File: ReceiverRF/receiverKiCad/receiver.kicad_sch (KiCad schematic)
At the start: 23 parts, among them J2 Conn_01x05_Socket, U1 STM32F103RET6, Y1 Crystal_GND24

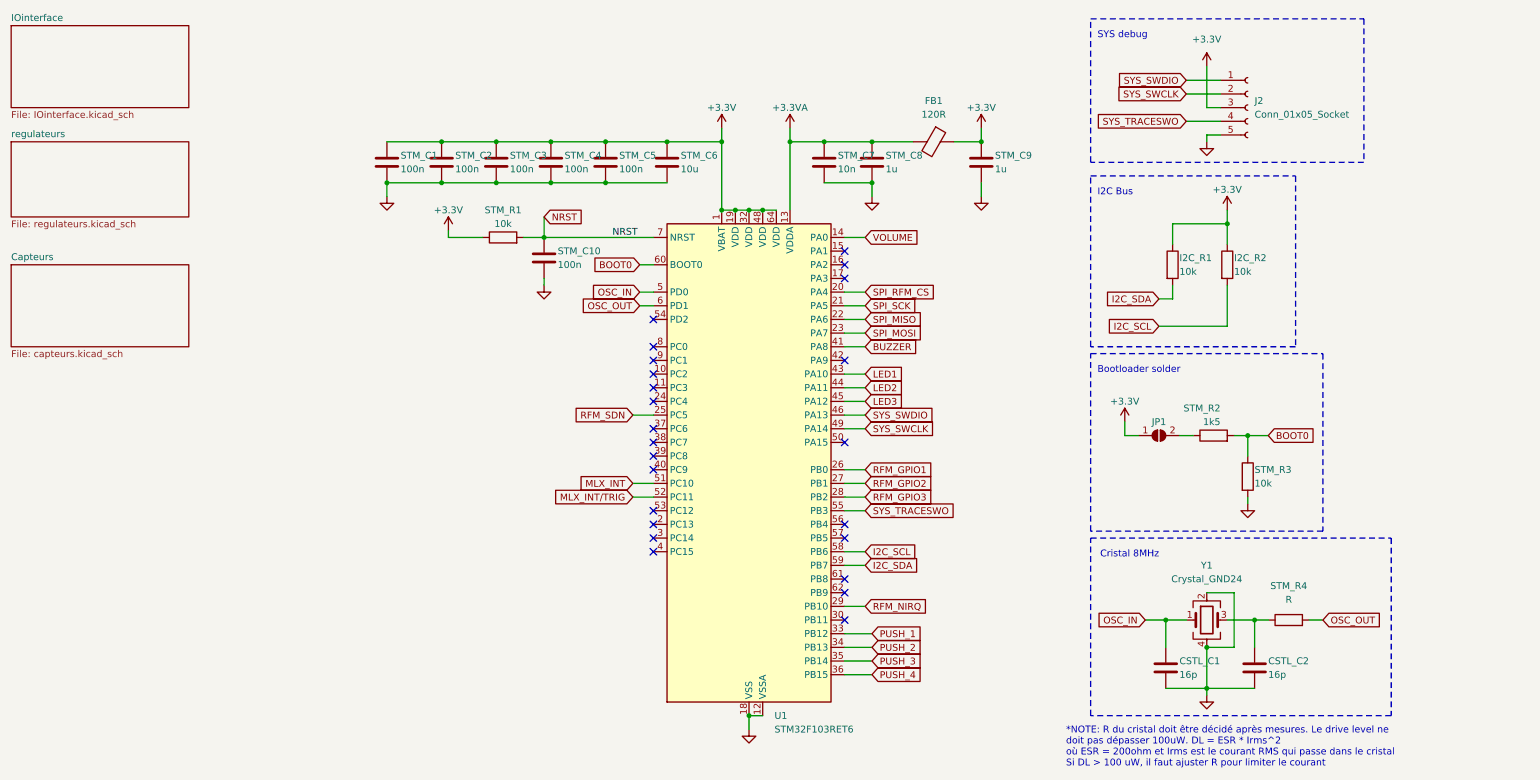
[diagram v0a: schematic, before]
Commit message: impédance 50 ohm pour l'Antenne
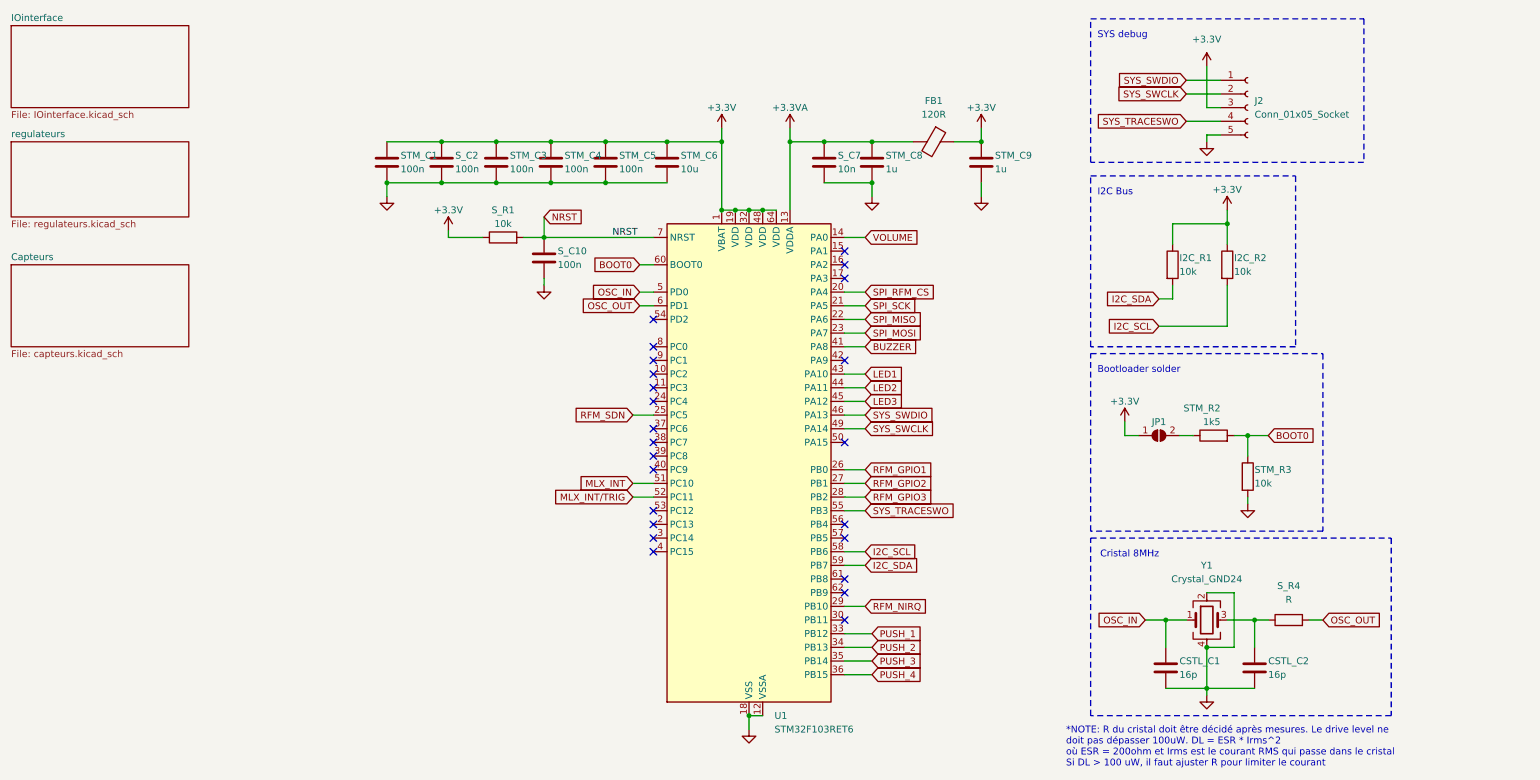
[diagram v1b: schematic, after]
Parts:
- renumbered STM_C10 to S_C10, STM_C2 to S_C2, STM_C7 to S_C7, STM_R1 to S_R1, STM_R4 to S_R4
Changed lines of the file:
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@@
 		(on_board yes)
 		(dnp no)
-		(property "Reference" "STM_R1"
+		(property "Reference" "S_R1"
 			(at 107.95 49.53 90)
 			(effects
@@
 			(project "receiver"
 				(path "/439ba515-58d4-4b14-87ab-b438dcf423a5"
-					(reference "STM_R1")
+					(reference "S_R1")
 					(unit 1)
 				)
@@
 		(on_board yes)
 		(dnp no)
-		(property "Reference" "STM_C2"
+		(property "Reference" "S_C2"
 			(at 99.06 39.37 0)
 			(effects
@@
 			(project "receiver"
 				(path "/439ba515-58d4-4b14-87ab-b438dcf423a5"
-					(reference "STM_C2")
+					(reference "S_C2")
 					(unit 1)
 				)
@@
 		(dnp no)
 		(fields_autoplaced yes)
-		(property "Reference" "STM_R4"
+		(property "Reference" "S_R4"
 			(at 254 119.38 90)
 			(effects
@@
 			(project "receiver"
 				(path "/439ba515-58d4-4b14-87ab-b438dcf423a5"
-					(reference "STM_R4")
+					(reference "S_R4")
 					(unit 1)
 				)
@@
 		(on_board yes)
 		(dnp no)
-		(property "Reference" "STM_C7"
+		(property "Reference" "S_C7"
 			(at 170.18 39.37 0)
 			(effects
@@
 			(project "receiver"
 				(path "/439ba515-58d4-4b14-87ab-b438dcf423a5"
-					(reference "STM_C7")
+					(reference "S_C7")
 					(unit 1)
 				)
@@
 		(on_board yes)
 		(dnp no)
-		(property "Reference" "STM_C10"
+		(property "Reference" "S_C10"
 			(at 118.11 57.15 0)
 			(effects
@@
 			(project "receiver"
 				(path "/439ba515-58d4-4b14-87ab-b438dcf423a5"
-					(reference "STM_C10")
-					(unit 1)
-				)
+					(reference "S_C10")
+					(unit 1)
+				)

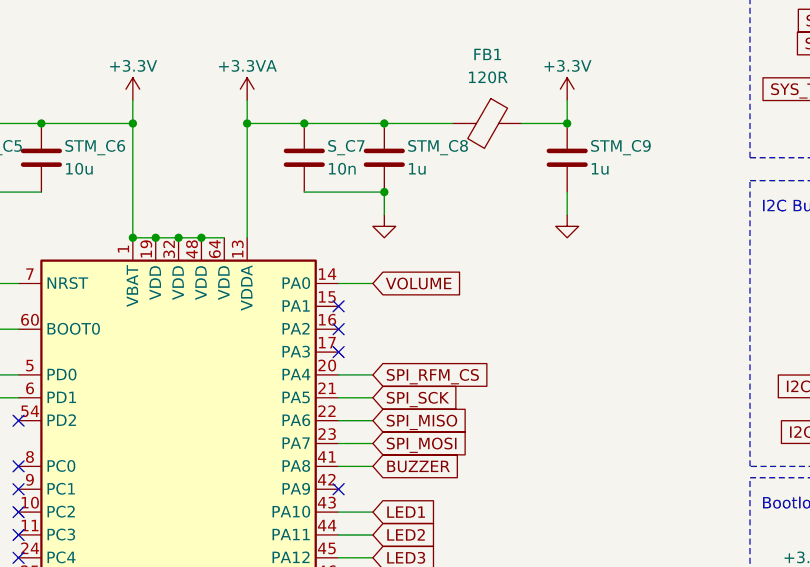
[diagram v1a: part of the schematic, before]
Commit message: changement circuit volume du buzzer. Ajustement du volume direct plutot que software.
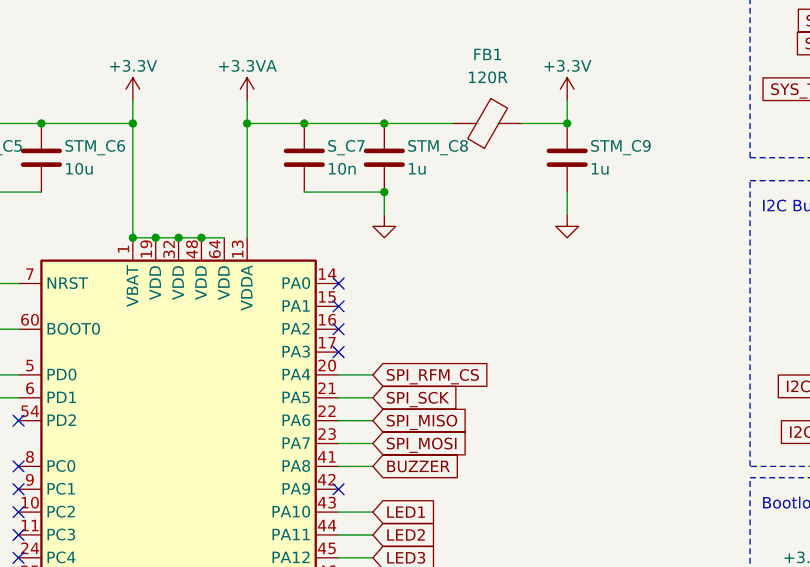
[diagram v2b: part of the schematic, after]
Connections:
- net VOLUME: no longer names the net of U1.14 (PA0)
- no-connect marks 24 -> 25
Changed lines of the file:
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@@
+	)
+	(no_connect
+		(at 135.89 95.25)
+	)
+	(no_connect
+		(at 171.45 59.69)
+	)
+	(no_connect
+		(at 171.45 77.47)
+	)
+	(no_connect
+		(at 135.89 105.41)
+	)
+	(no_connect
+		(at 135.89 85.09)
+	)
+	(no_connect
+		(at 135.89 110.49)
+	)
+	(no_connect
+		(at 171.45 120.65)
 	)
 	(no_connect
@@
 	)
 	(no_connect
-		(at 135.89 95.25)
-	)
-	(no_connect
-		(at 171.45 59.69)
-	)
-	(no_connect
-		(at 171.45 77.47)
-	)
-	(no_connect
-		(at 135.89 105.41)
-	)
-	(no_connect
-		(at 135.89 85.09)
-	)
-	(no_connect
-		(at 135.89 110.49)
-	)
-	(no_connect
-		(at 171.45 120.65)
-	)
-	(no_connect
 		(at 135.89 97.79)
 	)
@@
 	)
 	(no_connect
+		(at 171.45 54.61)
+	)
+	(no_connect
 		(at 135.89 113.03)
 	)
@@
 		(pts
 			(xy 171.45 67.31) (xy 175.26 67.31)
-		)
-		(stroke
-			(width 0)
-			(type default)
-		)
-	)
-	(wire
-		(pts
-			(xy 171.45 54.61) (xy 175.26 54.61)
 		)
 		(stroke
@@
 			(effects
 				(font
-					(size 1.27 1.27)
-				)
-				(justify left)
-				(hide yes)
-			)
-		)
-	)
-	(global_label "VOLUME"
-		(shape input)
-		(at 175.26 54.61 0)
-		(fields_autoplaced yes)
-		(effects
-			(font
-				(size 1.27 1.27)
-			)
-			(justify left)
-		)
-		(property "Intersheetrefs" "${INTERSHEET_REFS}"
-			(at 185.6233 54.61 0)
-			(effects
-				(font

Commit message: minor changes
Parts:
- S_R4: value R -> 10R
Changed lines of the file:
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@@
 			)
 		)
-		(property "Value" "R"
+		(property "Value" "10R"
 			(at 254 121.92 90)
 			(effects
